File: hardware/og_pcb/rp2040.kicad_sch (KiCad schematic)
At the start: 28 parts, among them J2 Conn_02x03_Top_Bottom, SW4 SW_Push_Shielded, SW5 SW_Push_Shielded, U1 254, U12 RP2040, U3 W25Q128JVS, Y3 ABM8-272-T3

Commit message: updated pcb work in progress (incomplete)
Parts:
- removed J2: Conn_02x03_Top_Bottom, Connector_Hirose:Hirose_DF11-6DP-2DSA_2x03_P2.00mm_Vertical, symbol Connector_Generic:Conn_02x03_Top_Bottom
- added J11: Conn_02x02_Top_Bottom, 1my_footprints:CON4_2X2_UF_DF11_HIR, symbol Connector_Generic:Conn_02x02_Top_Bottom
- added J4: Micro_SD_Card_Det1, symbol Connector:Micro_SD_Card_Det1
- added R4: 10k, Resistor_SMD:R_0402_1005Metric, symbol Device:R
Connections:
- net Power Monitor SCL is gone; now on net Temp Alert: U12.8 (GPIO6)
- net +3.3V: now also R4.1
- net GND: now also J11.3 (Pin_3), J11.4 (Pin_4)
- net MicroSD CS: now also R4.2
- net SWCLK: now also J11.1 (Pin_1)
- net SWD: now also J11.2 (Pin_2)
- net Temp Alert: no longer U12.31 (GPIO20)
- net SDA0: now reaches U12.6 (GPIO4)
- net SCL0: now reaches U12.7 (GPIO5)
- net Cosmic1 SDA: no longer names the net of U12.35 (GPIO23)
- net Cosmic2 SCL: no longer names the net of U12.36 (GPIO24)
- net IMU SCL/SPC: no longer names the net of U12.30 (GPIO19)
- net IMU SDA/SDI/SCO: no longer names the net of U12.29 (GPIO18)
- net Power Monitor SDA: no longer names the net of U12.9 (GPIO7)
- net RF DIO4: no longer names the net of U12.11 (GPIO8)
- net RF MISO: no longer names the net of U12.15 (GPIO12)
- net RF MOSI renamed SCL1
- net RF NSS: no longer names the net of U12.12 (GPIO9)
- net RF Reset: no longer names the net of U12.16 (GPIO13)
- net RF SCK renamed SDA1
- net SCL General: no longer names the net of U12.28 (GPIO17)
- net SDA General: no longer names the net of U12.27 (GPIO16)
- net Temp SCL: no longer names the net of U12.32 (GPIO21)
- net Temp SDA: no longer names the net of U12.34 (GPIO22)
- no-connect marks 8 -> 6
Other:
- note added: "I2C0: Temperature Sensor utilizing 5k pullup resistors I2C1: Everything else using 10k pullup resistors"
- note added: "dont need breakout board"
- note added: "might want to remove (dont need to send usb signals"
- note added: "pullup resistor"
- moved on the sheet: C6, D4, R23, R3, SW5, U1, U3

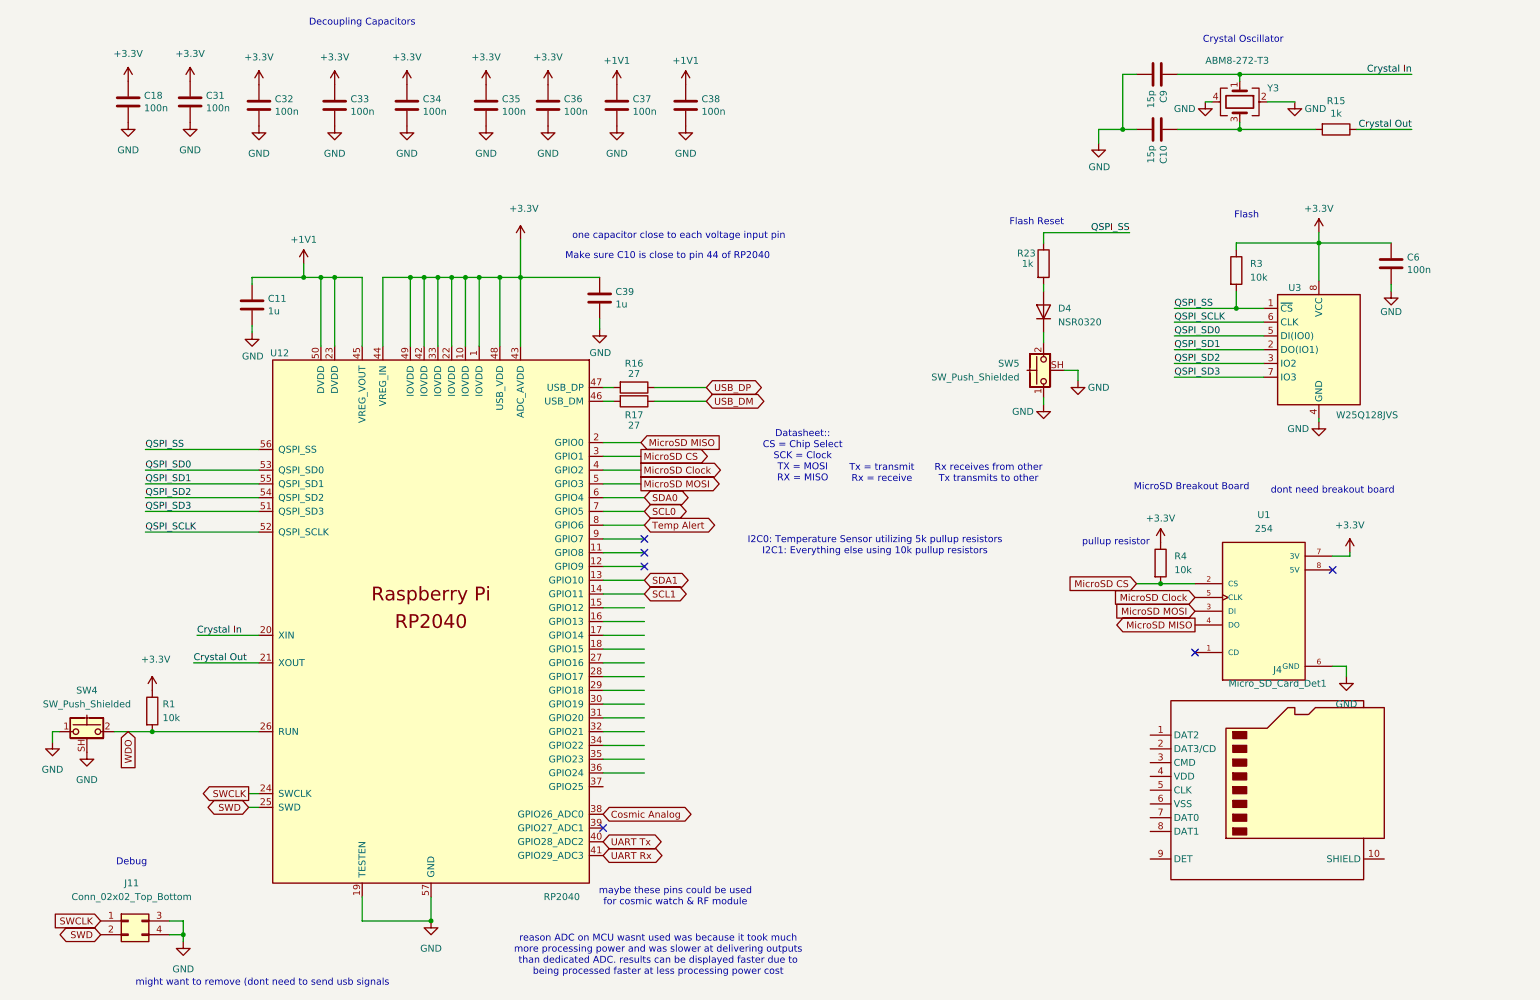
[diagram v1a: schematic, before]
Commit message: updated pcb v2 progress
reimplemented spi microSD, changed power monitor to model with internal shunt resistor, changed power supply from usbc to barrel jack, reconnected vbus to microusb, modified spi and i2c connections (2 i2c connections, 2 spi connections), removed RF module & IMU.

to do:
- find/create footprints for new parts
- verify implementation by reviewing datasheets again
- implement coax connector for analog connection to cosmic watch
- implement gps receiver (must do more research; implement one well-known/documented/used b4)
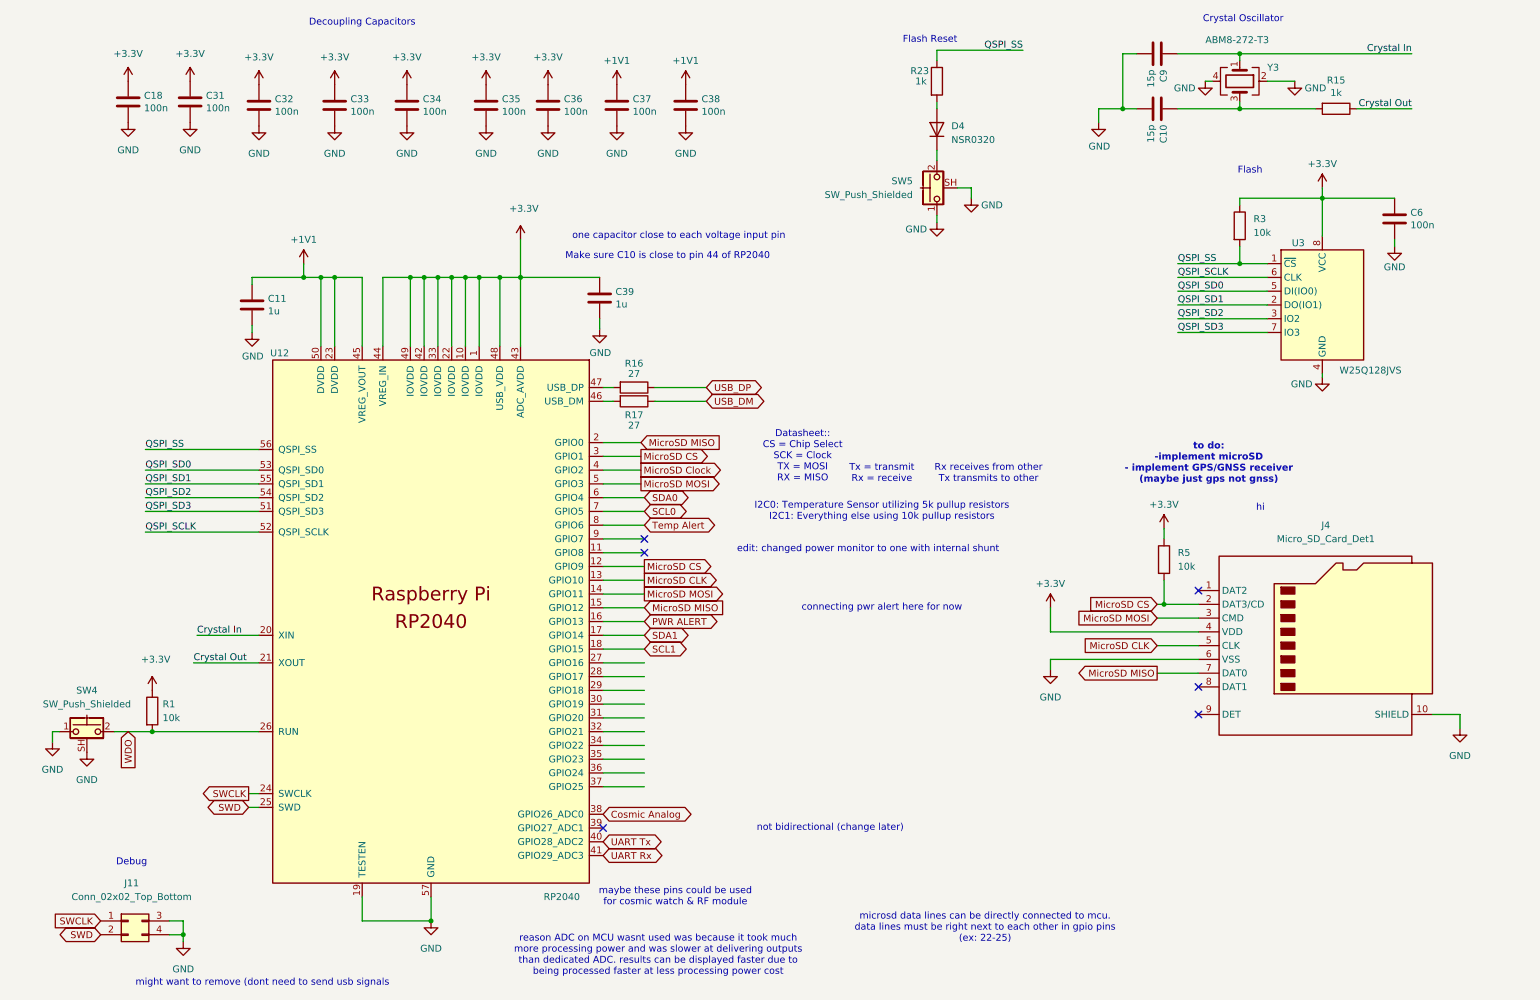
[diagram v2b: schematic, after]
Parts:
- removed R4: 10k, Resistor_SMD:R_0402_1005Metric, symbol Device:R
- removed U1: 254, 1my_footprints:MODULE_254, symbol 254:254
- added R5: 10k, Resistor_SMD:R_0402_1005Metric, symbol Device:R
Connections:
- net +3.3V: now also J4.4 (VDD), R5.1
- net GND: now also J4.10 (SHIELD), J4.6 (VSS)
- net MicroSD CS: now also J4.2 (DAT3/CD), U12.12 (GPIO9), R5.2
- net MicroSD MISO: now also J4.7 (DAT0), U12.15 (GPIO12)
- net MicroSD MOSI: now also J4.3 (CMD), U12.14 (GPIO11)
- net SCL1: now also U12.18 (GPIO15); no longer U12.14 (GPIO11)
- net SDA1: now also U12.17 (GPIO14); no longer U12.13 (GPIO10)
- net MicroSD CLK: now reaches J4.5 (CLK)
- net MicroSD CLK: now also U12.13 (GPIO10)
- net PWR ALERT: now reaches U12.16 (GPIO13)
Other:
- note added: "connecting pwr alert here for now"
- note added: "edit: changed power monitor to one with internal shunt"
- note added: "hi"
- note added: "microsd data lines can be directly connected to mcu. data lines must be right next to each other in gpio pins (ex: 22-25)"
- note added: "not bidirectional (change later)"
- note added: "to do: -implement microSD - implement GPS/GNSS receiver (maybe just gps not gnss)"
- note removed: "MicroSD Breakout Board"
- note removed: "dont need breakout board"
- note removed: "pullup resistor"
- moved on the sheet: C10, C6, C9, D4, J4, R15, R23, R3, SW5, U3, Y3

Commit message: new preliminary demo pcb
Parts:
- J4: footprint (none) -> 1my_footprints:microSD-503398-1892-1
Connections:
- net MicroSD Clock is gone; now on net MicroSD CLK: U12.4 (GPIO2)
- net MicroSD CLK: no longer U12.13 (GPIO10)
- net MicroSD CS: no longer U12.12 (GPIO9)
- net MicroSD MISO: no longer U12.15 (GPIO12)
- net MicroSD MOSI: no longer U12.14 (GPIO11)
- new net GPS Reset: U12.15 (GPIO12)
- no-connect marks 6 -> 19
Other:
- note added: "connecting pwr alert and gps reset here for now"
- note added: "to my knowledge, alert pins can be connected to any of the GPIO pins"
- note removed: "connecting pwr alert here for now"
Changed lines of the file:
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@@
 		)
 	)
+	(text "to my knowledge, alert pins can be connected to any of the GPIO pins"
+		(exclude_from_sim no)
+		(at 163.83 138.43 0)
+		(effects
+			(font
+				(size 1.27 1.27)
+			)
+		)
+	)
 	(text "Flash"
 		(exclude_from_sim no)
@@
 		)
 	)
-	(text "connecting pwr alert here for now"
+	(text "connecting pwr alert and gps reset here for now"
 		(exclude_from_sim no)
-		(at 168.91 126.365 0)
+		(at 167.005 127.635 0)
 		(effects
 			(font
@@
 	)
 	(no_connect
+		(at 125.095 154.305)
+	)
+	(no_connect
 		(at 227.33 146.05)
 	)
 	(no_connect
+		(at 125.095 149.225)
+	)
+	(no_connect
+		(at 125.095 159.385)
+	)
+	(no_connect
 		(at 125.095 116.205)
 	)
 	(no_connect
+		(at 125.095 146.685)
+	)
+	(no_connect
 		(at 125.095 113.665)
 	)
@@
 	)
 	(no_connect
+		(at 125.095 136.525)
+	)
+	(no_connect
+		(at 125.095 139.065)
+	)
+	(no_connect
+		(at 125.095 123.825)
+	)
+	(no_connect
 		(at 227.33 140.97)
 	)
 	(no_connect
+		(at 125.095 118.745)
+	)
+	(no_connect
+		(at 125.095 144.145)
+	)
+	(no_connect
+		(at 125.095 121.285)
+	)
+	(no_connect
+		(at 125.095 151.765)
+	)
+	(no_connect
 		(at 227.33 123.19)
 	)
+	(no_connect
+		(at 125.095 156.845)
+	)
+	(no_connect
+		(at 125.095 141.605)
+	)
 	(wire
 		(pts
@@
 		)
 	)
-	(global_label "MicroSD CS"
-		(shape output)
-		(at 125.095 118.745 0)
-		(fields_autoplaced yes)
-		(effects
-			(font
-				(size 1.27 1.27)
-			)
-			(justify left)
-		)
-		(property "Intersheetrefs" "${INTERSHEET_REFS}"
-			(at 139.0868 118.745 0)
-			(effects
-				(font
-					(size 1.27 1.27)
-				)
-				(justify left)
-				(hide yes)
-			)
-		)
-	)
 	(global_label "MicroSD MOSI"
 		(shape input)
@@
 		)
 	)
-	(global_label "MicroSD CLK"
-		(shape output)
-		(at 125.095 121.285 0)
-		(fields_autoplaced yes)
-		(effects
-			(font
-				(size 1.27 1.27)
-			)
-			(justify left)
-		)
-		(property "Intersheetrefs" "${INTERSHEET_REFS}"
-			(at 140.1754 121.285 0)
-			(effects
-				(font
-					(size 1.27 1.27)
-				)
-				(justify left)
-				(hide yes)
-			)
-		)
-	)
 	(global_label "SDA1"
 		(shape bidirectional)
@@
 		)
 	)
-	(global_label "Cosmic Analog"
-		(shape bidirectional)
-		(at 117.475 164.465 0)
+	(global_label "GPS Reset"
+		(shape output)
+		(at 125.095 126.365 0)
 		(fields_autoplaced yes)
 		(effects
@@
 		)
 		(property "Intersheetrefs" "${INTERSHEET_REFS}"
-			(at 135.7227 164.465 0)
+			(at 137.9983 126.365 0)
 			(effects
 				(font
@@
 		)
 	)
-	(global_label "MicroSD CS"
-		(shape input)
-		(at 219.71 125.73 180)
-		(fields_autoplaced yes)
-		(effects
-			(font
-				(size 1.27 1.27)
-			)
-			(justify right)
-		)
-		(property "Intersheetrefs" "${INTERSHEET_REFS}"
-			(at 205.7182 125.73 0)
-			(effects
-				(font
-					(size 1.27 1.27)
-				)
-				(justify right)
-				(hide yes)
-			)
-		)
-	)
-	(global_label "MicroSD MISO"
-		(shape input)
-		(at 125.095 126.365 0)
+	(global_label "MicroSD CLK"
+		(shape output)
+		(at 124.46 100.965 0)
 		(fields_autoplaced yes)
 		(effects
@@
 		)
 		(property "Intersheetrefs" "${INTERSHEET_REFS}"
-			(at 141.2035 126.365 0)
+			(at 139.5404 100.965 0)
 			(effects
 				(font
@@
 		)
 	)
-	(global_label "PWR ALERT"
+	(global_label "Cosmic Analog"
 		(shape bidirectional)
-		(at 125.095 128.905 0)
+		(at 117.475 164.465 0)
 		(fields_autoplaced yes)
 		(effects
 			(font
 				(size 1.27 1.27)
-				(thickness 0.1588)
 			)
 			(justify left)
 		)
 		(property "Intersheetrefs" "${INTERSHEET_REFS}"
-			(at 139.6538 128.905 0)
+			(at 135.7227 164.465 0)
 			(effects
 				(font
@@
 		)
 	)
-	(global_label "MicroSD CLK"
+	(global_label "MicroSD CS"
 		(shape input)
-		(at 219.71 133.35 180)
+		(at 219.71 125.73 180)
 		(fields_autoplaced yes)
 		(effects
@@
 		)
 		(property "Intersheetrefs" "${INTERSHEET_REFS}"
-			(at 204.6296 133.35 0)
+			(at 205.7182 125.73 0)
 			(effects
 				(font
@@
 		)
 	)
-	(global_label "UART Tx"
+	(global_label "PWR ALERT"
 		(shape bidirectional)
-		(at 117.475 169.545 0)
+		(at 125.095 128.905 0)
 		(fields_autoplaced yes)
 		(effects
 			(font
 				(size 1.27 1.27)
+				(thickness 0.1588)
 			)
 			(justify left)
 		)
 		(property "Intersheetrefs" "${INTERSHEET_REFS}"
-			(at 129.1915 169.545 0)
+			(at 139.6538 128.905 0)
 			(effects
 				(font
@@
 		)
 	)
-	(global_label "SCL0"
-		(shape bidirectional)
-		(at 125.095 108.585 0)
+	(global_label "MicroSD CLK"
+		(shape input)
+		(at 219.71 133.35 180)
 		(fields_autoplaced yes)
 		(effects
@@
 				(size 1.27 1.27)
 			)
-			(justify left)
+			(justify right)
 		)
 		(property "Intersheetrefs" "${INTERSHEET_REFS}"
-			(at 133.9086 108.585 0)
+			(at 204.6296 133.35 0)
 			(effects
 				(font
 					(size 1.27 1.27)
 				)
-				(justify left)
+				(justify right)
 				(hide yes)
 			)
 		)
 	)
-	(global_label "MicroSD MOSI"
-		(shape output)
-		(at 125.095 123.825 0)
+	(global_label "UART Tx"
+		(shape bidirectional)
+		(at 117.475 169.545 0)
 		(fields_autoplaced yes)
 		(effects
@@
 		)
 		(property "Intersheetrefs" "${INTERSHEET_REFS}"
-			(at 141.2035 123.825 0)
+			(at 129.1915 169.545 0)
 			(effects
 				(font
@@
 		)
 	)
-	(global_label "SDA0"
+	(global_label "SCL0"
 		(shape bidirectional)
-		(at 125.095 106.045 0)
+		(at 125.095 108.585 0)
 		(fields_autoplaced yes)
 		(effects
@@
 		)
 		(property "Intersheetrefs" "${INTERSHEET_REFS}"
-			(at 133.9691 106.045 0)
+			(at 133.9086 108.585 0)
 			(effects
 				(font
@@
 		)
 	)
-	(global_label "MicroSD Clock"
-		(shape output)
-		(at 124.46 100.965 0)
+	(global_label "SDA0"
+		(shape bidirectional)
+		(at 125.095 106.045 0)
 		(fields_autoplaced yes)
 		(effects
@@
 		)
 		(property "Intersheetrefs" "${INTERSHEET_REFS}"
-			(at 141.1732 100.965 0)
+			(at 133.9691 106.045 0)
 			(effects
 				(font
@@
 			)
 		)
-		(property "Footprint" ""
+		(property "Footprint" "1my_footprints:microSD-503398-1892-1"
 			(at 302.26 115.57 0)
 			(effects
